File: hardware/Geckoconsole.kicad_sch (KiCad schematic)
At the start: 59 parts, among them J1 Conn_01x08_Male, J31 Conn_01x07_Female, J50 USB-C, J70 I²C, J71 I²C, J81 Conn_01x07, Q51 S8050, Q52 S8050, SW2 Reset, SW41 Rotary_Encoder_Switch, U1 ESP32-WROOM-32, U101 AMS1117-3.3, U2 CP2102, U70 VCNL4040M3OE

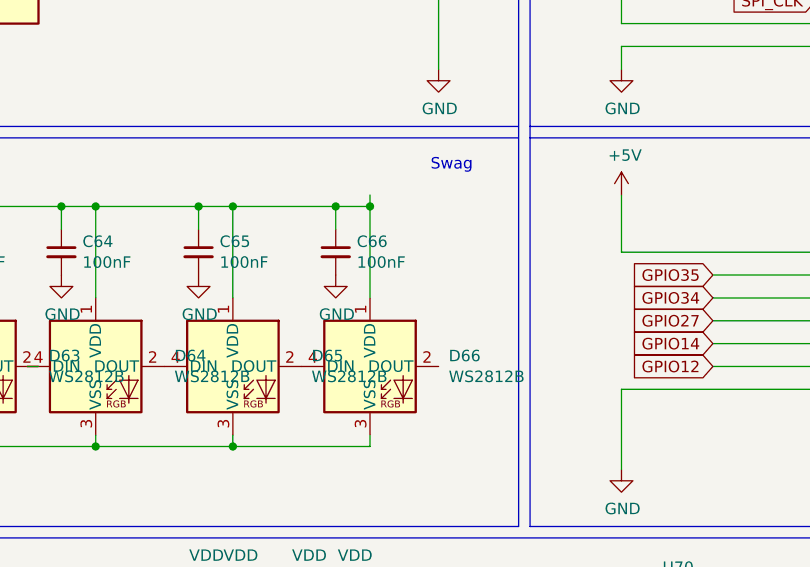
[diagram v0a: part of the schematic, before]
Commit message: Console Hardware: Fix DRC problems (unconnected traces etc.)
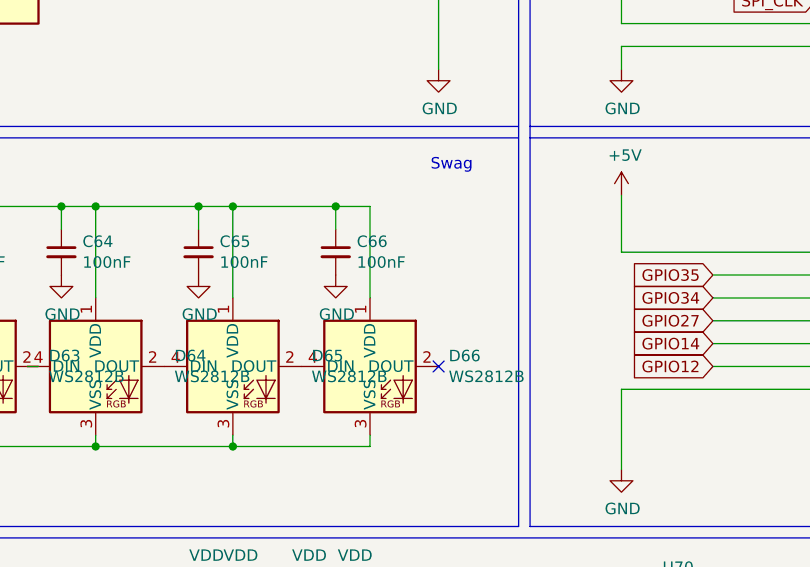
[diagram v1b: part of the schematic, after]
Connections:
- no-connect marks 30 -> 31

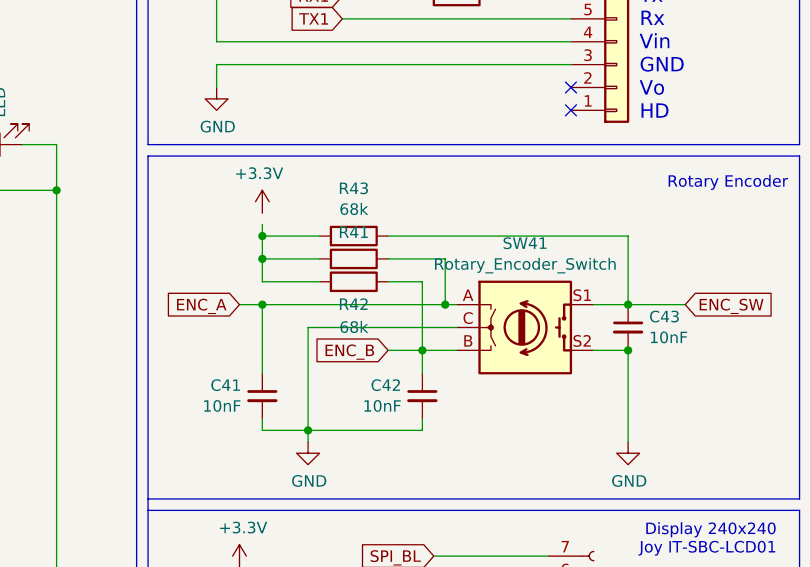
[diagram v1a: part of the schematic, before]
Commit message: Console Schema: Fix missing VCC connection on rotary enc
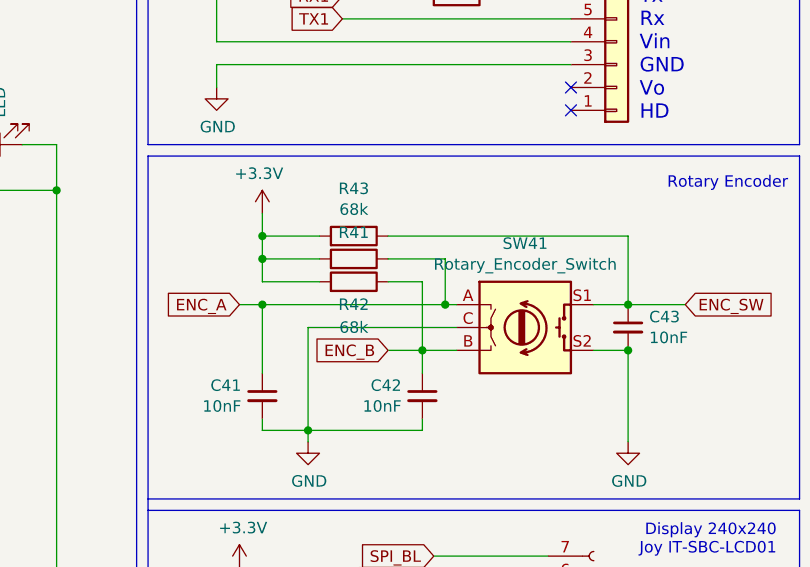
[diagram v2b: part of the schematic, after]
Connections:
- net +3V3: now also R41.2, R42.2, R43.2
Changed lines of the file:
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@@
     (stroke (width 0) (type default) (color 0 0 0 0))
   )
-  (wire (pts (xy 218.44 50.8) (xy 218.44 52.07))
+  (wire (pts (xy 218.44 49.53) (xy 218.44 52.07))
     (stroke (width 0) (type default) (color 0 0 0 0))
   )

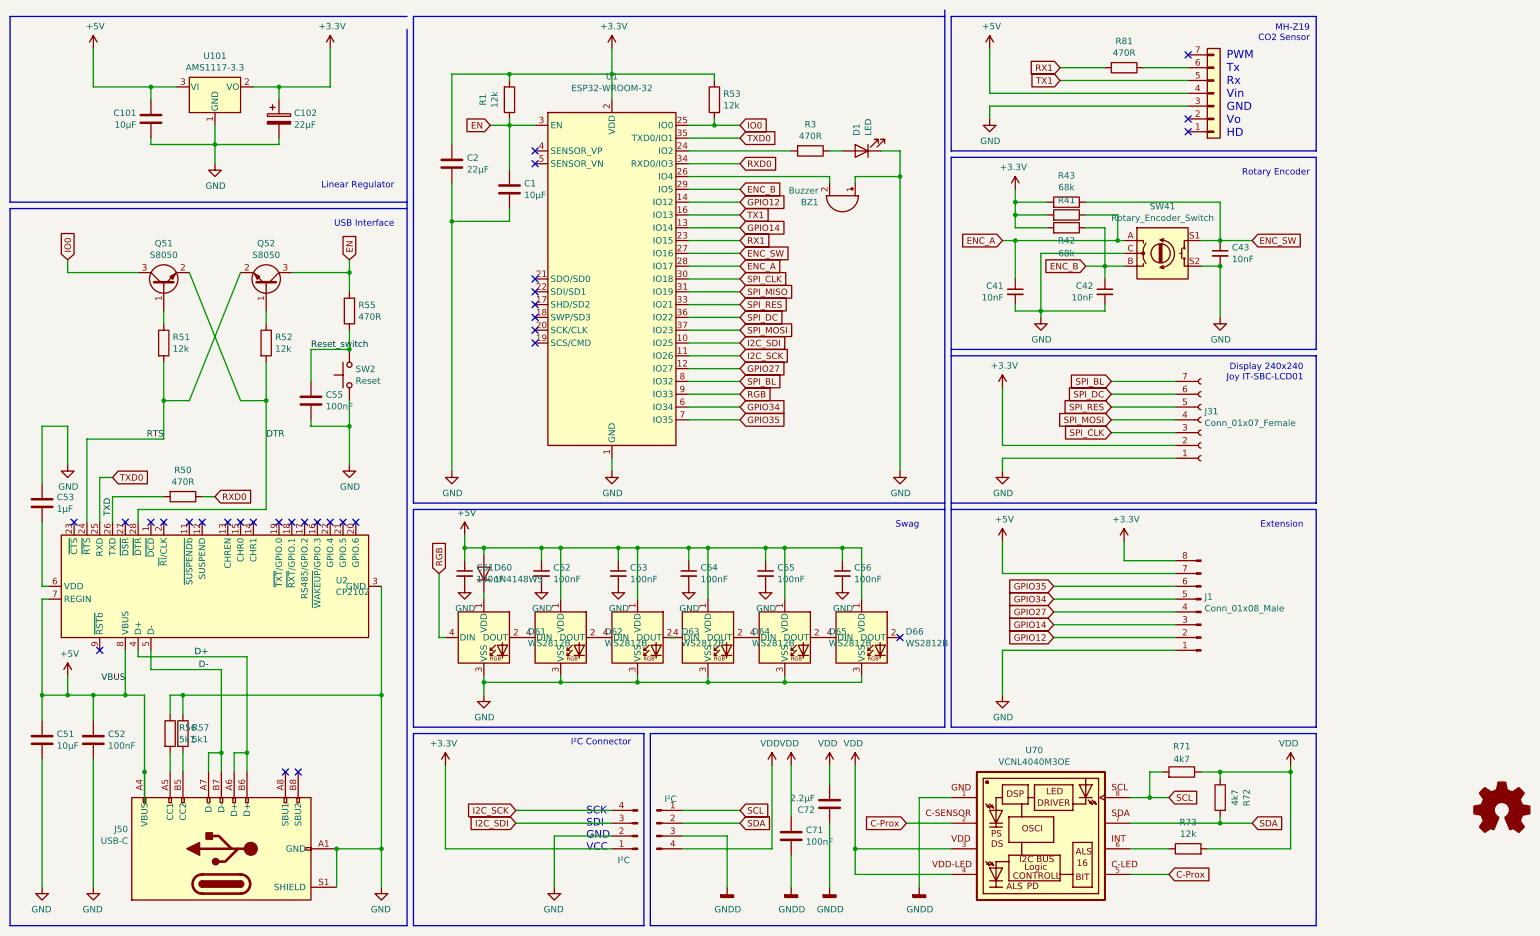
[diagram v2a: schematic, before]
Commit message: Schema Console: Additional Button2 for Navigation, remove R81
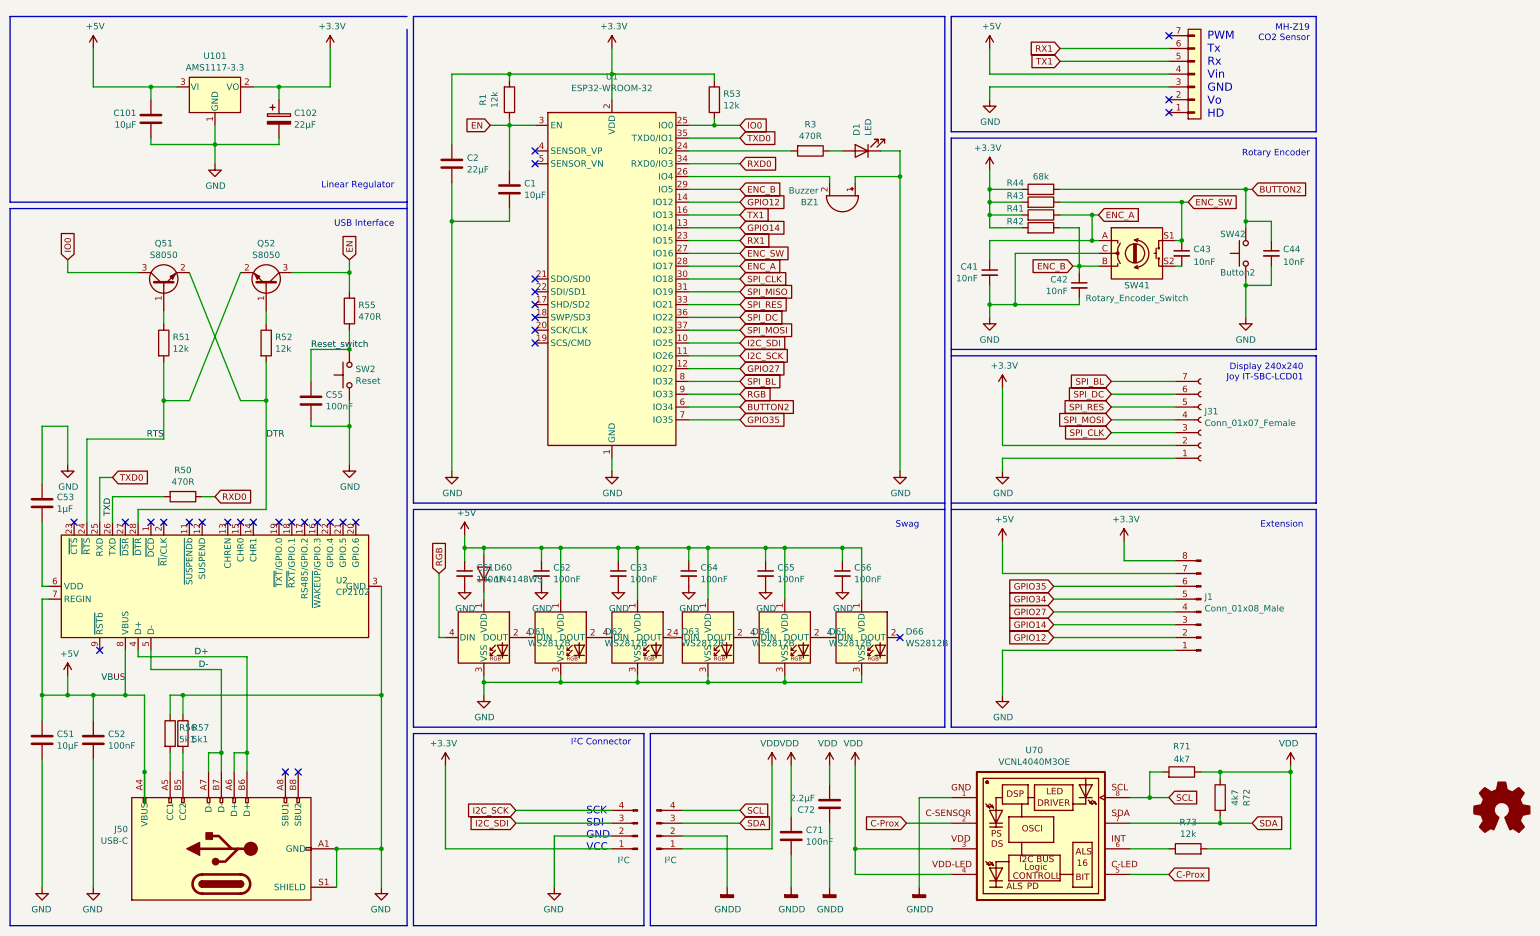
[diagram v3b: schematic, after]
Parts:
- removed R81: 470R, Resistor_SMD:R_0805_2012Metric_Pad1.20x1.40mm_HandSolder, symbol Device:R
- added C44: 10nF, Capacitor_SMD:C_0603_1608Metric_Pad1.08x0.95mm_HandSolder, symbol Device:C_Small
- added R44: 68k, Resistor_SMD:R_0805_2012Metric_Pad1.20x1.40mm_HandSolder, symbol Device:R
- added SW42: Button2, Button_Switch_SMD:SW_SPST_B3U-1000P-B, symbol Switch:SW_Push
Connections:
- net +3V3: now also R44.2
- net GND: now also C44.2, SW42.1; no longer C43.2, SW41.S2
- net GNDD: now also J71.2 (Pin_2); no longer J71.3 (Pin_3)
- net GPIO34: no longer U1.6 (IO34)
- net RX1: now also J81.6 (Pin_6)
- net SCL: now also J71.4 (Pin_4); no longer J71.1 (Pin_1)
- net SDA: now also J71.3 (Pin_3); no longer J71.2 (Pin_2)
- net VDD: now also J71.1 (Pin_1); no longer J71.4 (Pin_4)
- new net: C43.2, SW41.S2
- new net BUTTON2: C44.1, R44.1, SW42.2, U1.6 (IO34)
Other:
- moved on the sheet: C41, C42, C43, R41, R42, R43, SW41

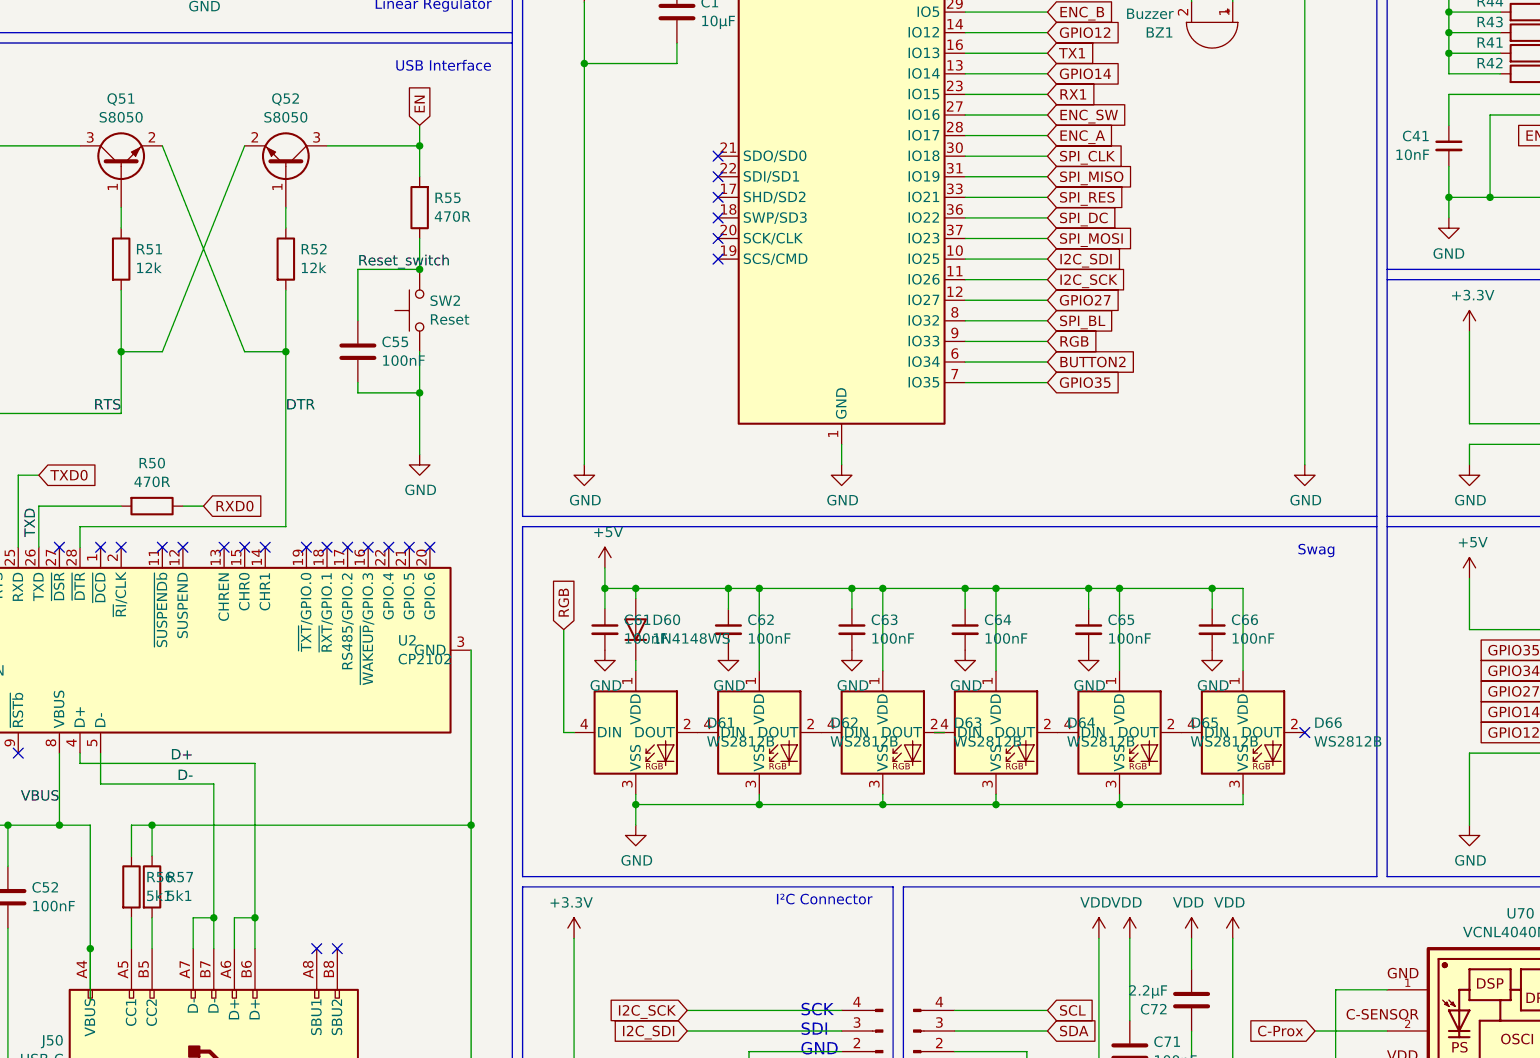
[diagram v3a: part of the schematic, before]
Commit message: Schema Console: Remove R55 (Fix Reset Button), graphical improvements
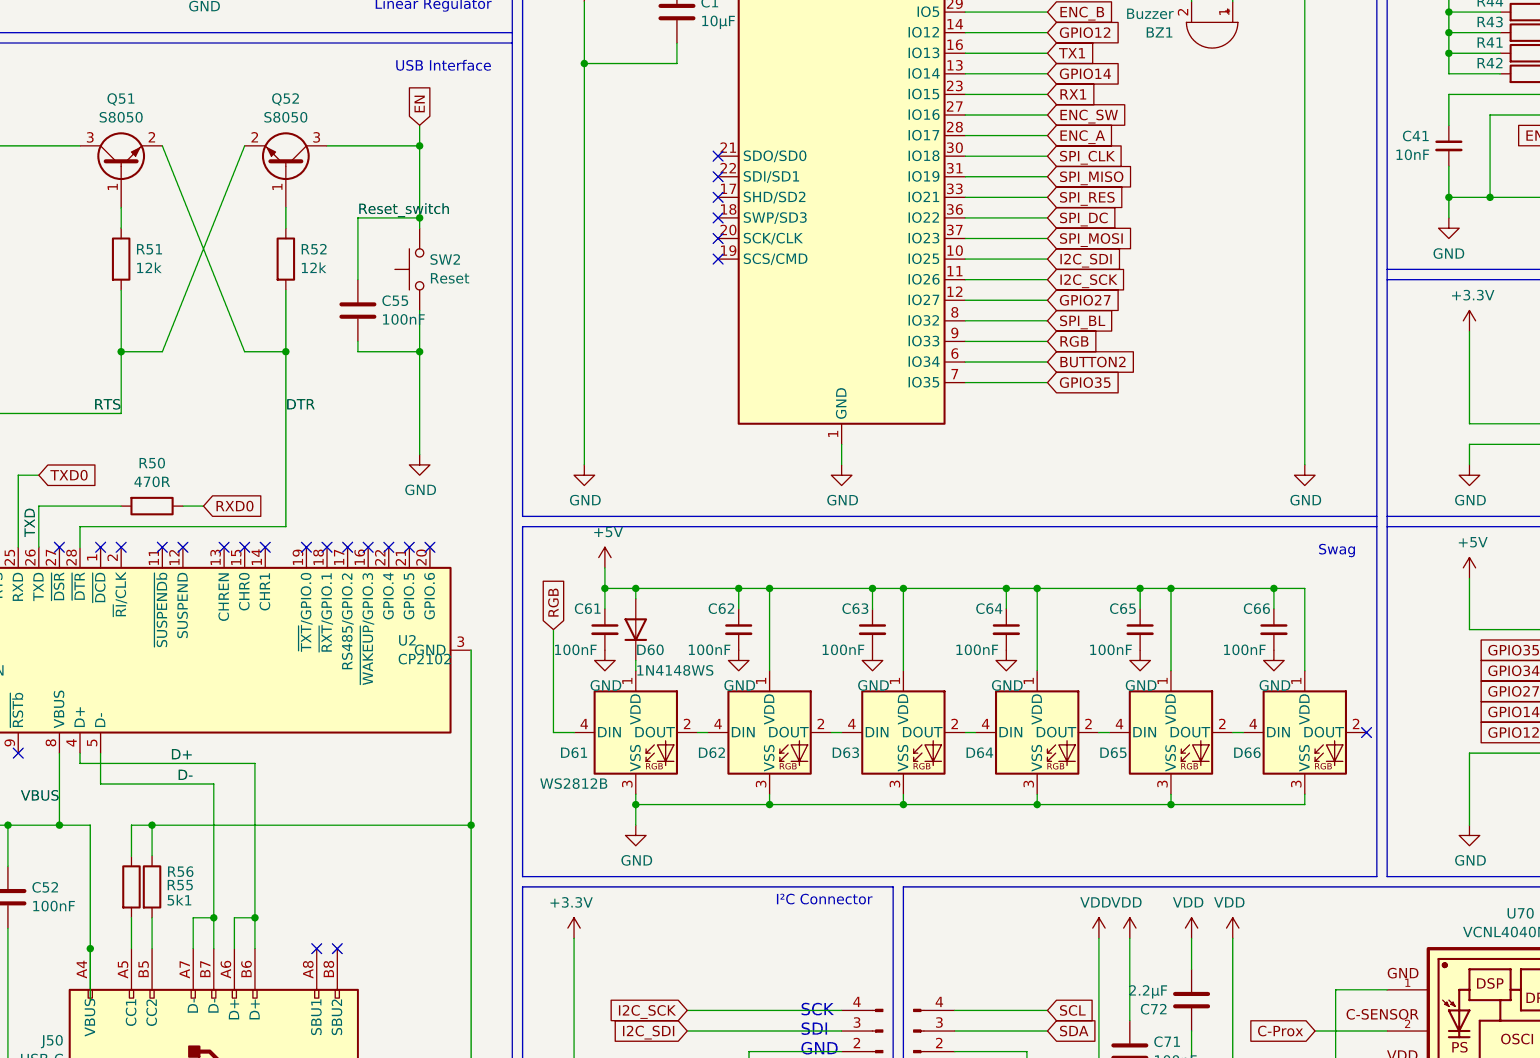
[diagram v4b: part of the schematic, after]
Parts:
- removed R55: 470R, Resistor_SMD:R_0805_2012Metric_Pad1.20x1.40mm_HandSolder, symbol Device:R
- renumbered R57 to R55
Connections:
- net Reset_switch is gone; now on net EN: C55.1, SW2.2
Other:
- moved on the sheet: C55, C62, C63, C64, C65, C66, D62, D63, D64, D65, D66, SW2
